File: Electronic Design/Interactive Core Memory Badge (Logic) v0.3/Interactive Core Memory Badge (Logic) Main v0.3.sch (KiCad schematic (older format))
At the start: 5 parts, among them J9 Conn_02x06_Odd_Even, U2 Teensy-LC, U7 SN74LV1T125DBVR

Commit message: Schematic refinement, header position checks.
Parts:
- J9: footprint Digikey:PinHeader_2x6_P2.54mm_Vertical_SMD -> Connector_PinHeader_2.54mm:PinHeader_2x06_P2.54mm_Vertical_SMD_and_TH
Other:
- note added: "I2C ADDRESS TABLE\nRequired\n IO EXPANDER 1: 32 decimal, 0x20\n IO EXPANDER 2: 33 decimal, 0x21\n HALL SENSOR 1: 48 decimal, 0x30\n HALL SENSOR 2: 49 decimal, 0x31\n HALL SENSOR 3: 50 decimal, 0x32\n HALL SENSOR 4: 51 decimal, 0x33\n EEPROM ID: 160 decimal, 0xA0\nOptional\n OLED: 60 decimal, 0x3C"
- note removed: "TO DO: I2C Address conflicts?\nRequired\n IO EXPANDER 1: 32 decimal, 0x20\n IO EXPANDER 2: 33 decimal, 0x21\n HALL SENSOR 1: 48 decimal, 0x30\n HALL SENSOR 2: 49 decimal, 0x31\n HALL SENSOR 3: 50 decimal, 0x32\n HALL SENSOR 4: 51 decimal, 0x33\nOptional\n OLED: 60 decimal, 0x3C"
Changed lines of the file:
@@
 IOEXP_ID33_INT_B
 Text Notes 800  6500 0    50   ~ 10
-TO DO: I2C Address conflicts?\nRequired\n  IO EXPANDER 1: 32 decimal, 0x20\n  IO EXPANDER 2: 33 decimal, 0x21\n  HALL SENSOR 1: 48 decimal, 0x30\n  HALL SENSOR 2: 49 decimal, 0x31\n  HALL SENSOR 3: 50 decimal, 0x32\n  HALL SENSOR 4: 51 decimal, 0x33\nOptional\n  OLED: 60 decimal, 0x3C
+I2C ADDRESS TABLE\nRequired\n  IO EXPANDER 1: 32 decimal, 0x20\n  IO EXPANDER 2: 33 decimal, 0x21\n  HALL SENSOR 1: 48 decimal, 0x30\n  HALL SENSOR 2: 49 decimal, 0x31\n  HALL SENSOR 3: 50 decimal, 0x32\n  HALL SENSOR 4: 51 decimal, 0x33\n  EEPROM ID: 160 decimal, 0xA0\nOptional\n  OLED: 60 decimal, 0x3C
 Text Notes 700  4100 0    50   ~ 0
 Try not to use any of these\nto avoid the need to populate\nthis end row header on the PCB.
@@
 F 0 "J9" H 9350 5370 50  0000 C CNN
 F 1 "Conn_02x06_Odd_Even" H 9350 5277 50  0000 C CNN
-F 2 "Digikey:PinHeader_2x6_P2.54mm_Vertical_SMD" H 9300 4950 50  0001 C CNN
+F 2 "Connector_PinHeader_2.54mm:PinHeader_2x06_P2.54mm_Vertical_SMD_and_TH" H 9300 4950 50  0001 C CNN
 F 3 "~" H 9300 4950 50  0001 C CNN
 	1    9300 4950

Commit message: Footprint verification and refinement
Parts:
- J9: value Conn_02x06_Odd_Even -> TSM-106-03-T-DV‎
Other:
- note added: "TO DO: TEENSY requires at least three headers\nthat do not get auto populated in the BOM from KiCAD."
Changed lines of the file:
@@
 P 9300 4950
 F 0 "J9" H 9350 5370 50  0000 C CNN
-F 1 "Conn_02x06_Odd_Even" H 9350 5277 50  0000 C CNN
+F 1 "TSM-106-03-T-DV‎" H 9350 5277 50  0000 C CNN
 F 2 "Connector_PinHeader_2.54mm:PinHeader_2x06_P2.54mm_Vertical_SMD_and_TH" H 9300 4950 50  0001 C CNN
 F 3 "~" H 9300 4950 50  0001 C CNN
@@
 Wire Wire Line
 	8950 5150 8950 5250
+Text Notes 4450 2200 0    50   ~ 10
+TO DO: TEENSY requires at least three headers\nthat do not get auto populated in the BOM from KiCAD.
 $EndSCHEMATC

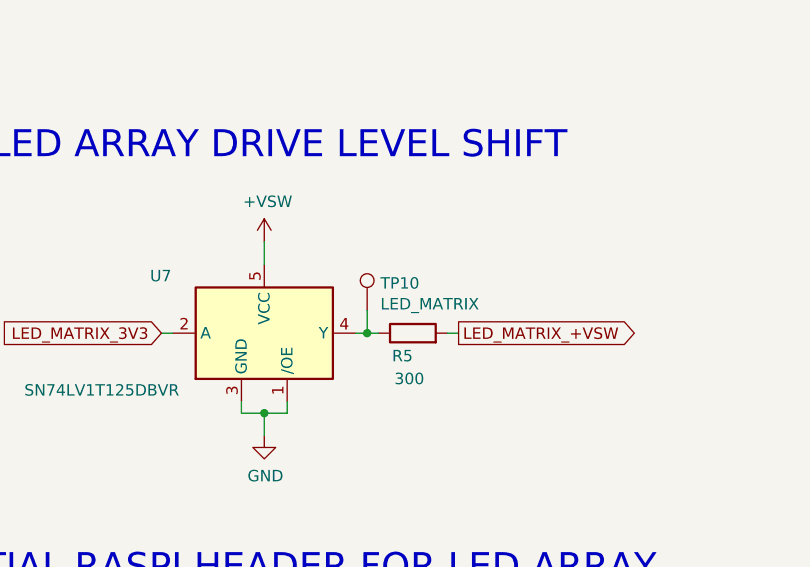
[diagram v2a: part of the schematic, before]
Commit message: Embiggen to 85x170mm
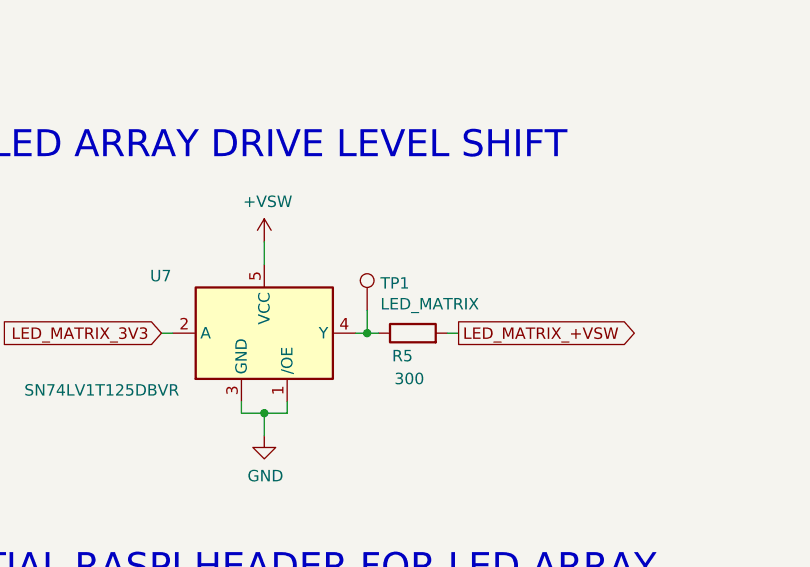
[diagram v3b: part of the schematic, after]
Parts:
- TP1: renamed from TP10; footprint TestPoint:TestPoint_Keystone_5000-5004_Miniature -> TestPoint:TestPoint_THTPad_D1.7mm_Drill1.0mm
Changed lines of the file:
@@
 AR Path="/5E755787/5EA33CB4" Ref="TP?"  Part="1"
 AR Path="/5E755AC8/5D2551FF/5EA33CB4" Ref="TP?"  Part="1"
-AR Path="/5EA33CB4" Ref="TP10"  Part="1"
-F 0 "TP10" H 9608 2968 50  0000 L CNN
+AR Path="/5EA33CB4" Ref="TP1"  Part="1"
+F 0 "TP1" H 9608 2968 50  0000 L CNN
 F 1 "LED_MATRIX" H 9608 2877 50  0000 L CNN
-F 2 "TestPoint:TestPoint_Keystone_5000-5004_Miniature" H 9750 2850 50  0001 C CNN
+F 2 "TestPoint:TestPoint_THTPad_D1.7mm_Drill1.0mm" H 9750 2850 50  0001 C CNN
 F 3 "~" H 9750 2850 50  0001 C CNN
 	1    9550 2850

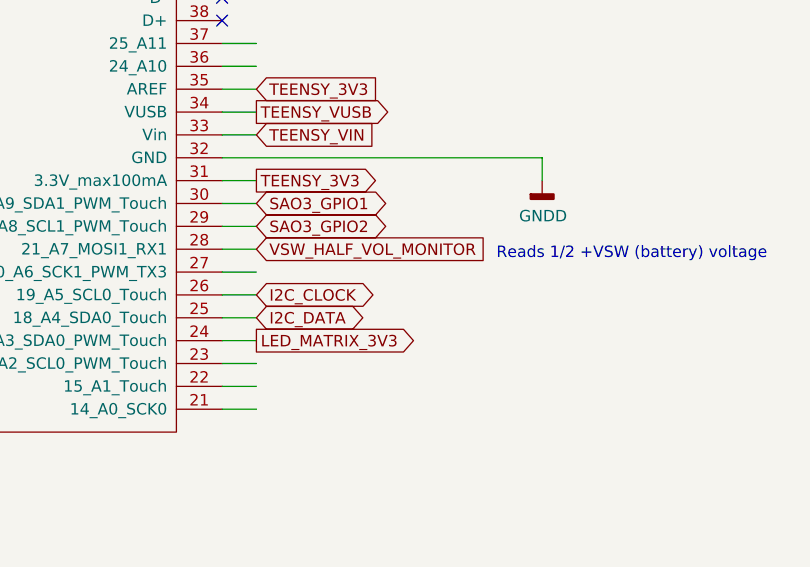
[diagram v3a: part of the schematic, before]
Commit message: Update library refs (OneDrive to Dropbox)
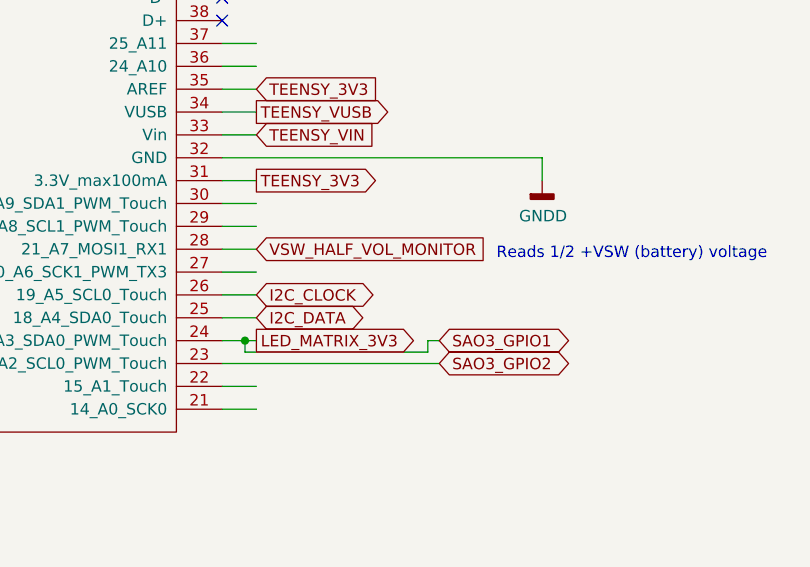
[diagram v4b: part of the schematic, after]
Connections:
- wire segments 49 -> 54
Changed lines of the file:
@@
 	4200 4200 4350 4200
-Wire Wire Line
-	4200 4100 4350 4100
 Wire Wire Line
 	4200 3700 4350 3700
@@
 I2C_DATA
 Wire Wire Line
-	4200 4000 4350 4000
+	4200 4000 4300 4000
 Text GLabel 4350 4000 2    50   Output ~ 0
 LED_MATRIX_3V3
@@
 Text GLabel 1900 3500 0    50   BiDi ~ 0
 SAO2_GPIO1(TX)
-Text GLabel 4350 3400 2    50   BiDi ~ 0
+Text GLabel 5150 4000 2    50   BiDi ~ 0
 SAO3_GPIO1
-Text GLabel 4350 3500 2    50   BiDi ~ 0
+Text GLabel 5150 4100 2    50   BiDi ~ 0
 SAO3_GPIO2
 Wire Wire Line
@@
 Text Notes 4450 2200 0    50   ~ 10
 TO DO: TEENSY requires at least three headers\nthat do not get auto populated in the BOM from KiCAD.
+Wire Wire Line
+	4300 4000 4300 4050
+Wire Wire Line
+	4300 4050 5100 4050
+Wire Wire Line
+	5100 4050 5100 4000
+Wire Wire Line
+	5100 4000 5150 4000
+Connection ~ 4300 4000
+Wire Wire Line
+	4300 4000 4350 4000
+Wire Wire Line
+	4200 4100 5150 4100
 $EndSCHEMATC

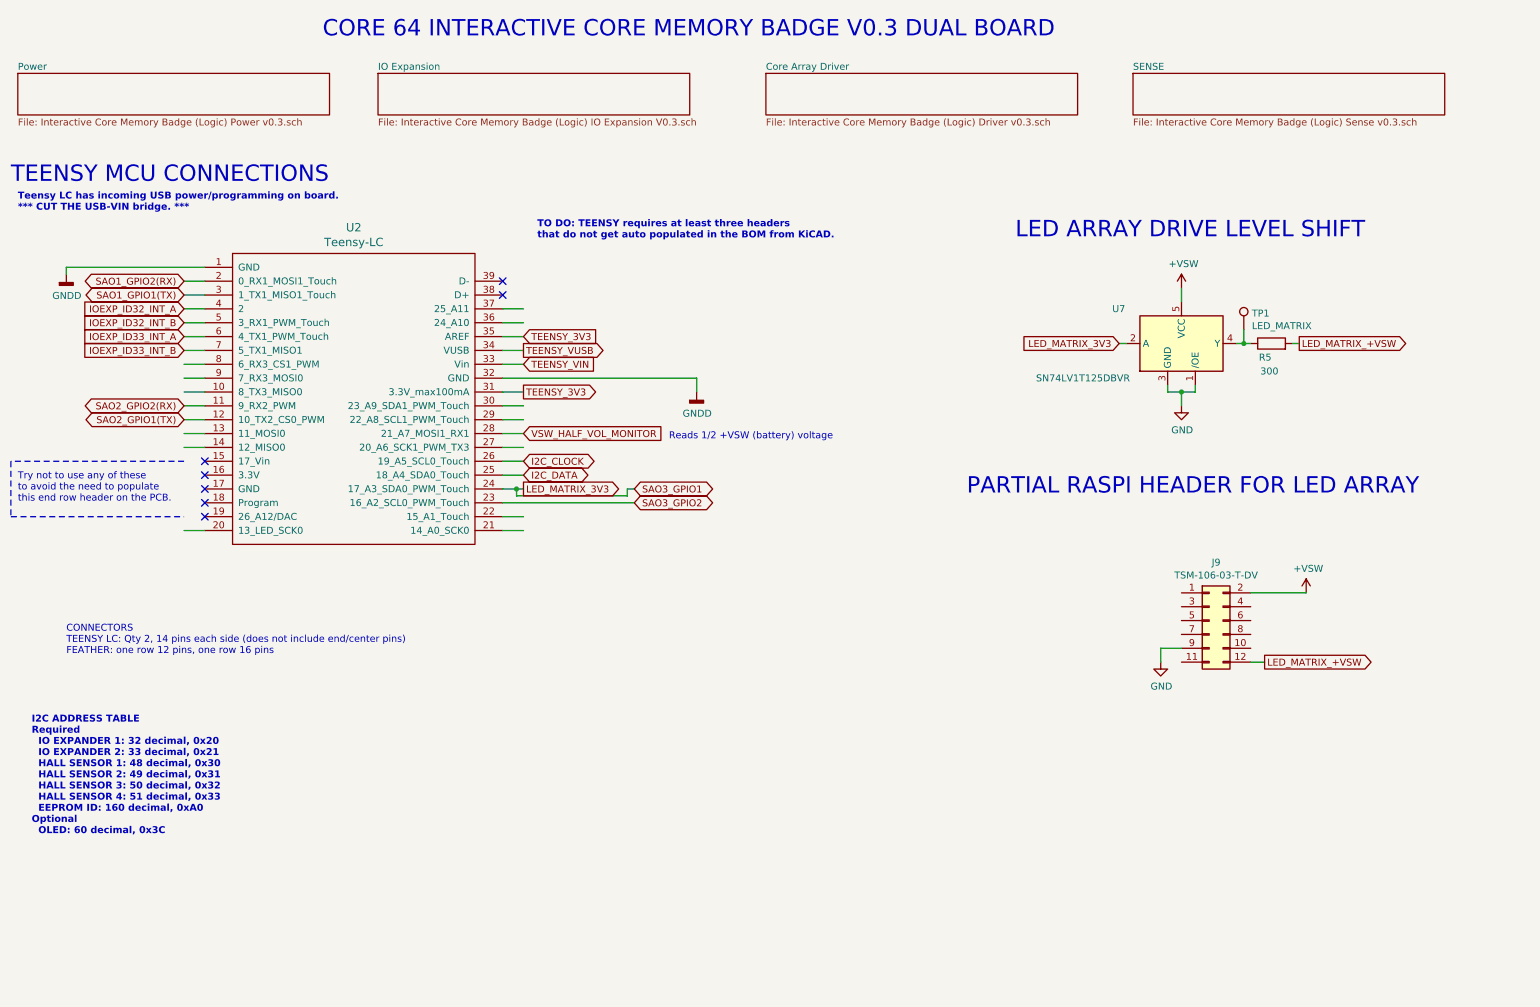
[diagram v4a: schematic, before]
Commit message: Board layout, PDFs for review
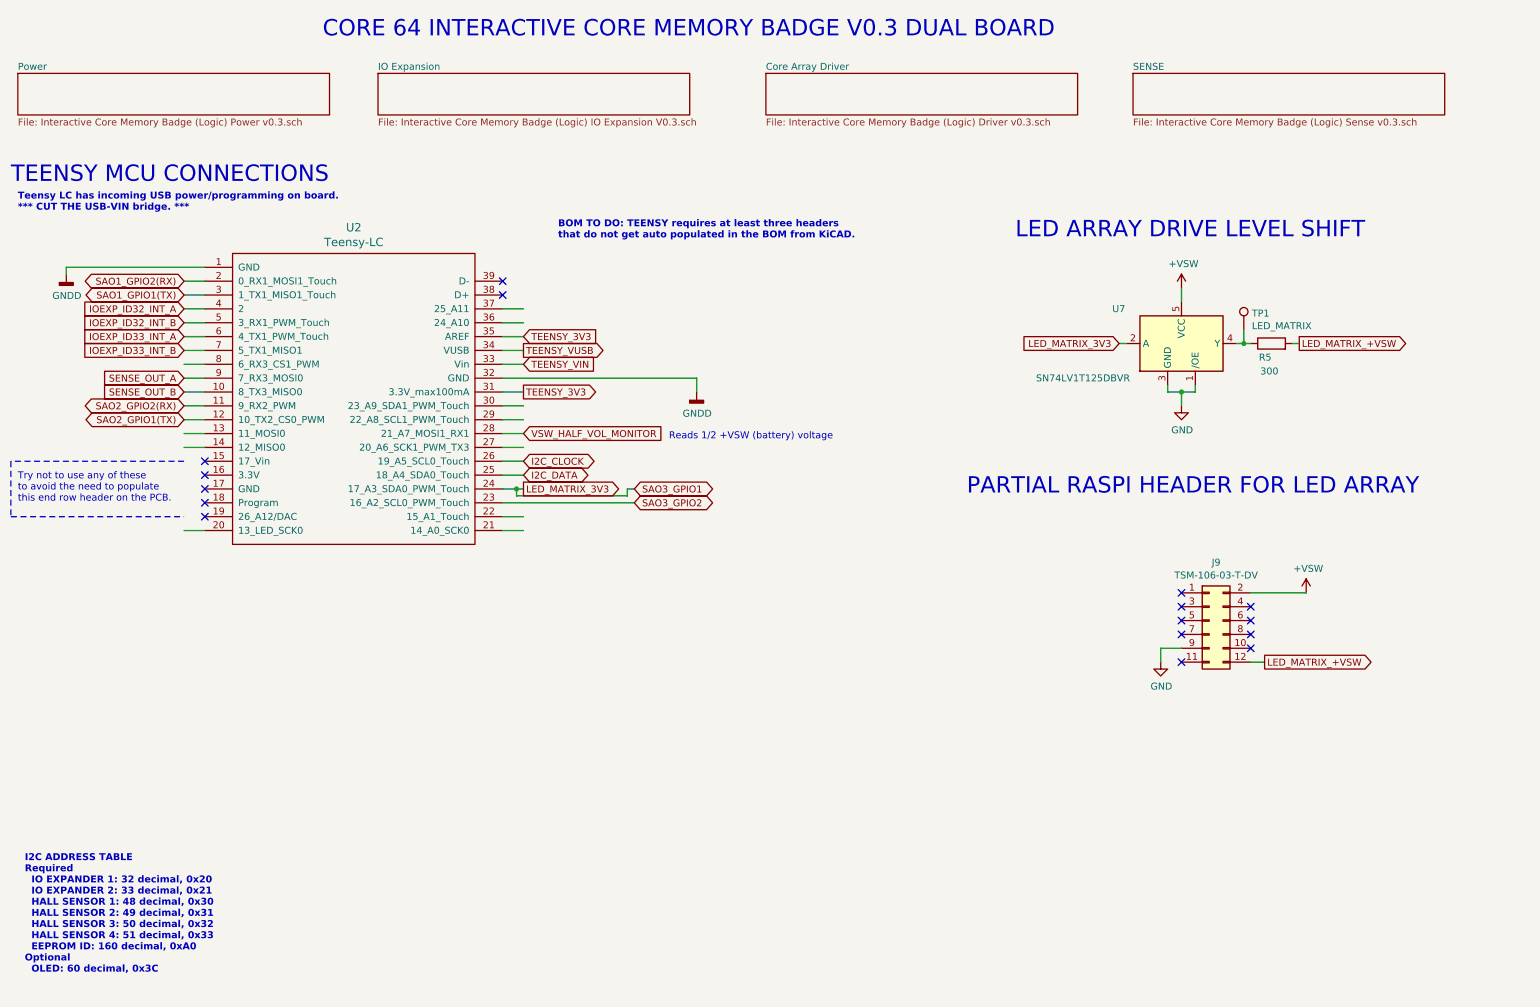
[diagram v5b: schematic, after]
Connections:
- net labels added: SENSE_OUT_A, SENSE_OUT_B
- no-connect marks 7 -> 16
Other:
- note added: "BOM TO DO: TEENSY requires at least three headers\nthat do not get auto populated in the BOM from KiCAD."
- note removed: "CONNECTORS\nTEENSY LC: Qty 2, 14 pins each side (does not include end/center pins)\nFEATHER: one row 12 pins, one row 16 pins"
- note removed: "TO DO: TEENSY requires at least three headers\nthat do not get auto populated in the BOM from KiCAD."
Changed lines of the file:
@@
 	4200 2700 4350 2700
 NoConn ~ 2050 3900
-Text Notes 1050 5200 0    50   ~ 0
-CONNECTORS\nTEENSY LC: Qty 2, 14 pins each side (does not include end/center pins)\nFEATHER: one row 12 pins, one row 16 pins
 $Comp
 L power:GNDD #PWR?
@@
 Text GLabel 1900 3000 0    50   Input ~ 0
 IOEXP_ID33_INT_B
-Text Notes 800  6500 0    50   ~ 10
+Text Notes 750  7500 0    50   ~ 10
 I2C ADDRESS TABLE\nRequired\n  IO EXPANDER 1: 32 decimal, 0x20\n  IO EXPANDER 2: 33 decimal, 0x21\n  HALL SENSOR 1: 48 decimal, 0x30\n  HALL SENSOR 2: 49 decimal, 0x31\n  HALL SENSOR 3: 50 decimal, 0x32\n  HALL SENSOR 4: 51 decimal, 0x33\n  EEPROM ID: 160 decimal, 0xA0\nOptional\n  OLED: 60 decimal, 0x3C
 Text Notes 700  4100 0    50   ~ 0
@@
 Wire Wire Line
 	8950 5150 8950 5250
-Text Notes 4450 2200 0    50   ~ 10
-TO DO: TEENSY requires at least three headers\nthat do not get auto populated in the BOM from KiCAD.
+Text Notes 4600 2200 0    50   ~ 10
+BOM TO DO: TEENSY requires at least three headers\nthat do not get auto populated in the BOM from KiCAD.
 Wire Wire Line
 	4300 4000 4300 4050
@@
 Wire Wire Line
 	4200 4100 5150 4100
+NoConn ~ 9600 4850
+NoConn ~ 9600 4950
+NoConn ~ 9600 5050
+NoConn ~ 9600 5150
+NoConn ~ 9100 5250
+NoConn ~ 9100 5050
+NoConn ~ 9100 4950
+NoConn ~ 9100 4850
+NoConn ~ 9100 4750
+Text GLabel 1900 3200 0    50   Input ~ 0
+SENSE_OUT_A
+Text GLabel 1900 3300 0    50   Input ~ 0
+SENSE_OUT_B
 $EndSCHEMATC

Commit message: Schematic review tweaks
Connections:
- net labels added: LED_MATRIX_+VSW_SIG, LED_MATRIX_3V3_SIG
- net labels removed: LED_MATRIX_+VSW, LED_MATRIX_3V3
- wire segments 54 -> 56
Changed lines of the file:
@@
 I2C_DATA
 Wire Wire Line
-	4200 4000 4300 4000
-Text GLabel 4350 4000 2    50   Output ~ 0
-LED_MATRIX_3V3
+	4200 4000 4650 4000
+Text GLabel 4750 4000 2    50   Output ~ 0
+LED_MATRIX_3V3_SIG
 Text GLabel 9950 2950 2    50   Output ~ 0
-LED_MATRIX_+VSW
+LED_MATRIX_+VSW_SIG
 $Comp
 L Connector:TestPoint TP?
@@
 	9500 2950 9550 2950
 Text GLabel 8650 2950 0    50   Input ~ 0
-LED_MATRIX_3V3
+LED_MATRIX_3V3_SIG
 Wire Wire Line
 	8650 2950 8700 2950
@@
 Text GLabel 1900 3500 0    50   BiDi ~ 0
 SAO2_GPIO1(TX)
-Text GLabel 5150 4000 2    50   BiDi ~ 0
+Text GLabel 5750 4000 2    50   BiDi ~ 0
 SAO3_GPIO1
-Text GLabel 5150 4100 2    50   BiDi ~ 0
+Text GLabel 5750 4200 2    50   BiDi ~ 0
 SAO3_GPIO2
 Wire Wire Line
@@
 $EndComp
 Text GLabel 9700 5250 2    50   Output ~ 0
-LED_MATRIX_+VSW
+LED_MATRIX_+VSW_SIG
 $Comp
 L power:GND #PWR?
@@
 BOM TO DO: TEENSY requires at least three headers\nthat do not get auto populated in the BOM from KiCAD.
 Wire Wire Line
-	4300 4000 4300 4050
-Wire Wire Line
-	4300 4050 5100 4050
-Wire Wire Line
-	5100 4050 5100 4000
-Wire Wire Line
-	5100 4000 5150 4000
-Connection ~ 4300 4000
-Wire Wire Line
-	4300 4000 4350 4000
-Wire Wire Line
-	4200 4100 5150 4100
+	4650 4000 4650 4100
+Wire Wire Line
+	4650 4100 5700 4100
+Wire Wire Line
+	5700 4100 5700 4000
+Wire Wire Line
+	5700 4000 5750 4000
+Connection ~ 4650 4000
+Wire Wire Line
+	4650 4000 4750 4000
+Wire Wire Line
+	4200 4100 4550 4100
 NoConn ~ 9600 4850
 NoConn ~ 9600 4950
@@
 Text GLabel 1900 3300 0    50   Input ~ 0
 SENSE_OUT_B
+Wire Wire Line
+	4550 4100 4550 4200
+Wire Wire Line
+	4550 4200 5750 4200
 $EndSCHEMATC

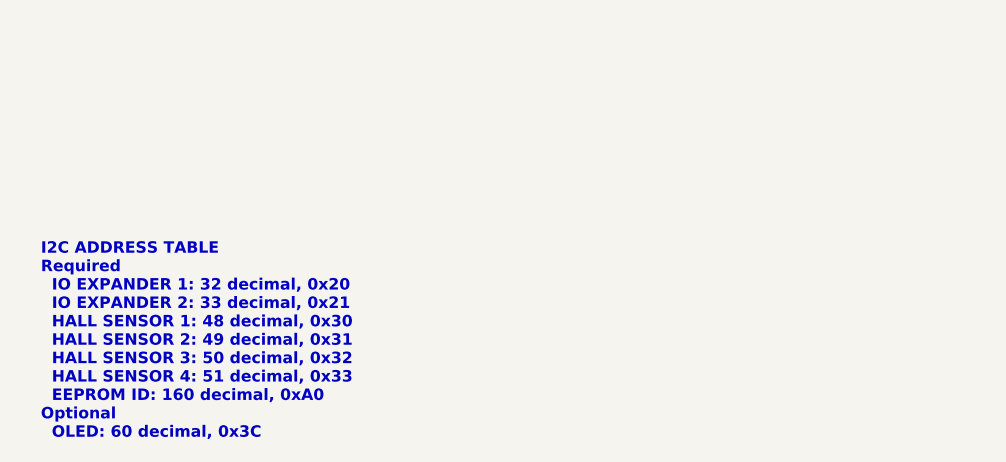
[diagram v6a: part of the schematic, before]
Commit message: I2C address updates
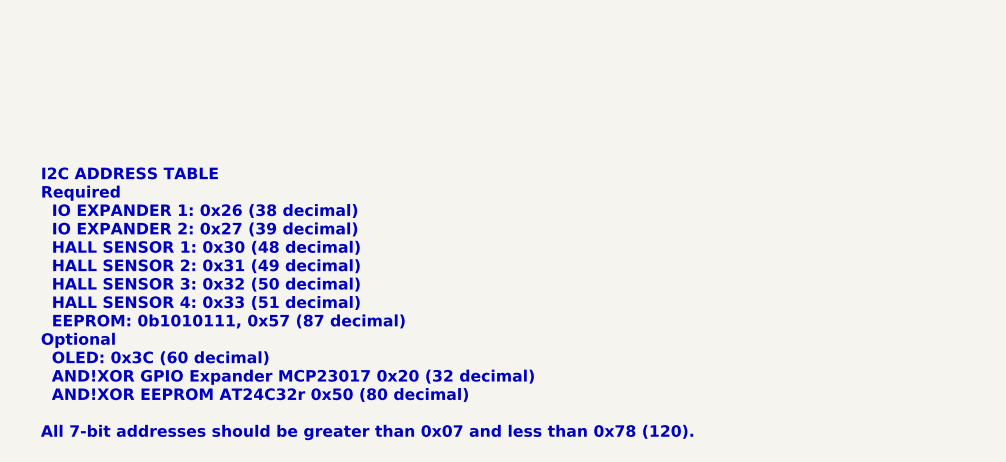
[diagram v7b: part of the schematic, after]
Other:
- note added: "I2C ADDRESS TABLE\nRequired\n IO EXPANDER 1: 0x26 (38 decimal)\n IO EXPANDER 2: 0x27 (39 decimal)\n HALL SENSOR 1: 0x30 (48 decimal)\n HALL SENSOR 2: 0x31 (49 decimal)\n HALL SENSOR 3: 0x32 (50 decimal)\n HALL SENSOR 4: 0x33 (51 decimal)\n EEPROM: 0b1010111, 0x57 (87 decimal)\nOptional\n OLED: 0x3C (60 decimal)\n AND!XOR GPIO Expander MCP23017 0x20 (32 decimal)\n AND!XOR EEPROM AT24C32r 0x50 (80 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"
- note removed: "I2C ADDRESS TABLE\nRequired\n IO EXPANDER 1: 32 decimal, 0x20\n IO EXPANDER 2: 33 decimal, 0x21\n HALL SENSOR 1: 48 decimal, 0x30\n HALL SENSOR 2: 49 decimal, 0x31\n HALL SENSOR 3: 50 decimal, 0x32\n HALL SENSOR 4: 51 decimal, 0x33\n EEPROM ID: 160 decimal, 0xA0\nOptional\n OLED: 60 decimal, 0x3C"
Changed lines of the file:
@@
 IOEXP_ID33_INT_B
 Text Notes 750  7500 0    50   ~ 10
-I2C ADDRESS TABLE\nRequired\n  IO EXPANDER 1: 32 decimal, 0x20\n  IO EXPANDER 2: 33 decimal, 0x21\n  HALL SENSOR 1: 48 decimal, 0x30\n  HALL SENSOR 2: 49 decimal, 0x31\n  HALL SENSOR 3: 50 decimal, 0x32\n  HALL SENSOR 4: 51 decimal, 0x33\n  EEPROM ID: 160 decimal, 0xA0\nOptional\n  OLED: 60 decimal, 0x3C
+I2C ADDRESS TABLE\nRequired\n  IO EXPANDER 1: 0x26 (38 decimal)\n  IO EXPANDER 2: 0x27 (39 decimal)\n  HALL SENSOR 1: 0x30 (48 decimal)\n  HALL SENSOR 2: 0x31 (49 decimal)\n  HALL SENSOR 3: 0x32 (50 decimal)\n  HALL SENSOR 4: 0x33 (51 decimal)\n  EEPROM: 0b1010111, 0x57 (87 decimal)\nOptional\n  OLED: 0x3C (60 decimal)\n  AND!XOR GPIO Expander MCP23017 0x20 (32 decimal)\n  AND!XOR EEPROM AT24C32r 0x50 (80 decimal)\n\nAll 7-bit addresses should be greater than 0x07 and less than 0x78 (120).
 Text Notes 700  4100 0    50   ~ 0
 Try not to use any of these\nto avoid the need to populate\nthis end row header on the PCB.
